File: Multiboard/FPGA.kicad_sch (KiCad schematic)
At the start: 68 parts, among them J6 Conn_02x20_Odd_Even, J7 Conn_02x20_Odd_Even, J8 USB_C_Receptacle_USB2.0_16P, U6 LCMXO2-1200ZE-1TG144C, U7 FAN1112, U8 NCP1117

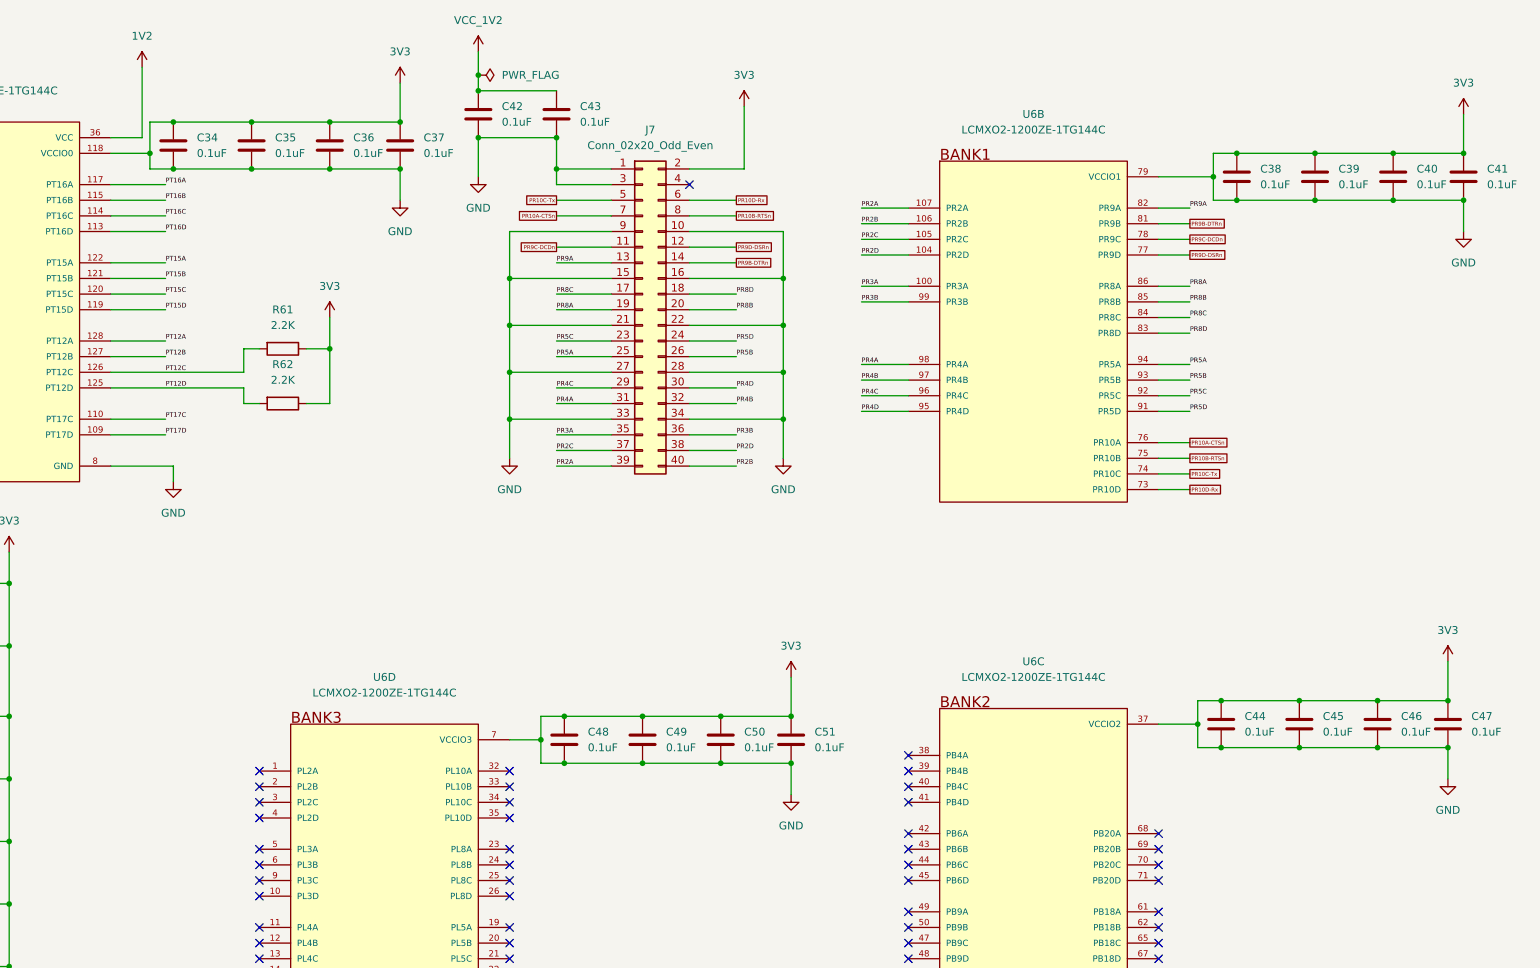
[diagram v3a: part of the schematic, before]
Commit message: Added footprints and fixed schematic
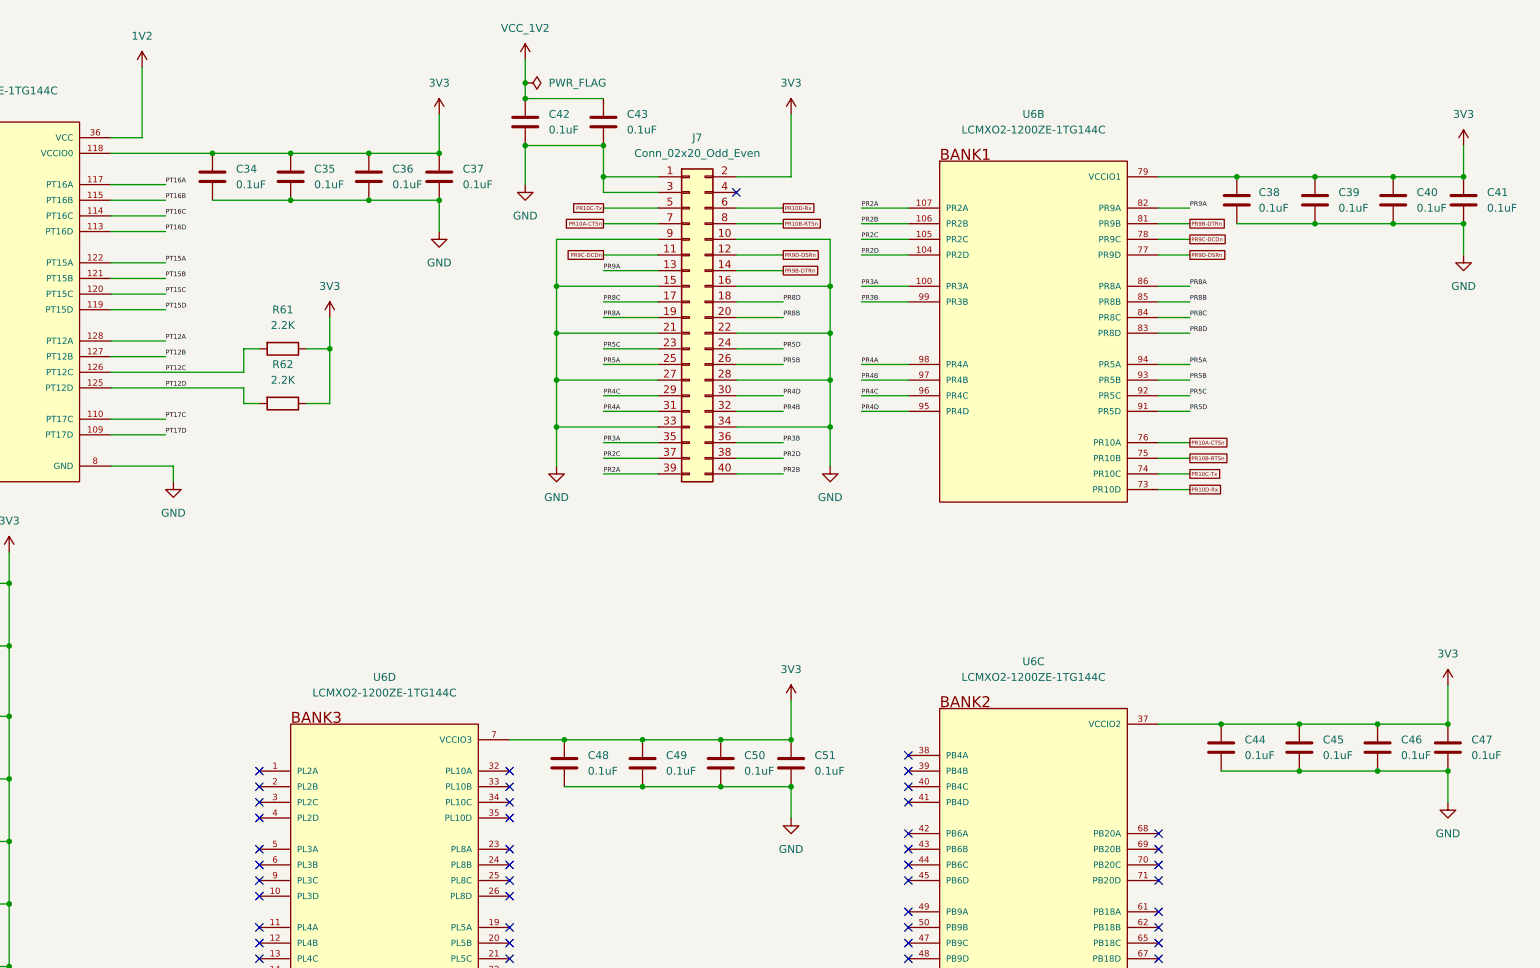
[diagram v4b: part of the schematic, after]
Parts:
- C34, C35, C36, C37, C38, C39, C40, C41, C42, C43, C44, C45, C46, C47, C48, C49, C50, C51, C52, C53, C54, C55, C56, C57, C58, C59, C60, C61, C62, C63, C64, C65, C66, C67: footprint (none) -> Capacitor_SMD:C_0603_1608Metric_Pad1.08x0.95mm_HandSolder
- D10, D11, D12, D13, D14, D15, D7, D8, D9: footprint (none) -> LED_SMD:LED_0603_1608Metric_Pad1.05x0.95mm_HandSolder
- R61, R62, R63, R64, R65, R66, R67, R68, R69, R70, R71, R72, R73, R74, R75, R76: footprint (none) -> Resistor_SMD:R_0603_1608Metric_Pad0.98x0.95mm_HandSolder
- U7, U8: footprint (none) -> Package_TO_SOT_SMD:SOT-223
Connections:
- net 3V3: no longer C34.2, C35.2, C36.2, C37.2, C38.2, C39.2, C40.2, C41.2, C42.2, C43.2, C44.2, C45.2, C46.2, C47.2, C48.2, C49.2, C50.2, C51.2, C52.2, C53.2, C54.2, C55.2, C56.2, C57.2, C58.2, C59.2, C60.2, C61.2, C62.2, C63.2, C64.2, C65.2, C66.2, C67.2, D7.1 (K), J6.15 (Pin_15), J6.16 (Pin_16), J6.23 (Pin_23), J6.24 (Pin_24), J6.31 (Pin_31), J6.32 (Pin_32), J6.39 (Pin_39), J6.40 (Pin_40), J6.7 (Pin_7), J6.8 (Pin_8), J7.1 (Pin_1), J7.10 (Pin_10), J7.15 (Pin_15), J7.16 (Pin_16), J7.21 (Pin_21), J7.22 (Pin_22), J7.27 (Pin_27), J7.28 (Pin_28), J7.3 (Pin_3), J7.33 (Pin_33), J7.34 (Pin_34), J7.9 (Pin_9), J8.A1 (GND), J8.A12 (GND), J8.B1 (GND), J8.B12 (GND), R63.1, R64.2, R65.2, U6.101 (GND), U6.116 (GND), U6.124 (GND), U6.134 (GND), U6.18 (GND), U6.29 (GND), U6.46 (GND), U6.53 (GND), U6.64 (GND), U6.8 (GND), U6.80 (GND), U6.90 (GND), U7.1 (GND), U8.1 (GND)
- new net GND: C34.2, C35.2, C36.2, C37.2, C38.2, C39.2, C40.2, C41.2, C42.2, C43.2, C44.2, C45.2, C46.2, C47.2, C48.2, C49.2, C50.2, C51.2, C52.2, C53.2, C54.2, C55.2, C56.2, C57.2, C58.2, C59.2, C60.2, C61.2, C62.2, C63.2, C64.2, C65.2, C66.2, C67.2, D7.1 (K), J6.15 (Pin_15), J6.16 (Pin_16), J6.23 (Pin_23), J6.24 (Pin_24), J6.31 (Pin_31), J6.32 (Pin_32), J6.39 (Pin_39), J6.40 (Pin_40), J6.7 (Pin_7), J6.8 (Pin_8), J7.1 (Pin_1), J7.10 (Pin_10), J7.15 (Pin_15), J7.16 (Pin_16), J7.21 (Pin_21), J7.22 (Pin_22), J7.27 (Pin_27), J7.28 (Pin_28), J7.3 (Pin_3), J7.33 (Pin_33), J7.34 (Pin_34), J7.9 (Pin_9), J8.A1 (GND), J8.A12 (GND), J8.B1 (GND), J8.B12 (GND), R63.1, R64.2, R65.2, U6.101 (GND), U6.116 (GND), U6.124 (GND), U6.134 (GND), U6.18 (GND), U6.29 (GND), U6.46 (GND), U6.53 (GND), U6.64 (GND), U6.8 (GND), U6.80 (GND), U6.90 (GND), U7.1 (GND), U8.1 (GND)
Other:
- moved on the sheet: C34, C35, C36, C37, C38, C39, C40, C41, C42, C43, C44, C45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
